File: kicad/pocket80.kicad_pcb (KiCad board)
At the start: 4 copper layers, 68.6 x 107.3 mm, 144 parts, among them J1 USB_C_Receptacle_USB2.0_14P, J2 Conn_02x10_Odd_Even, J3 Conn_01x02, Q1 IRLML6402, Q2 BC847, SW1 F1, SW10 4, SW11 9, SW12 5, SW13 A, SW14 6, SW15 B, SW16 7, SW17 0, SW18 INC, SW19 1, SW2 F2, SW20 DEC, SW21 2, SW22 SEL, SW23 3, SW24 GO!, SW25 SW_Push_DPDT, SW26 RESET, SW3 F3, SW4 F4, SW5 C, SW6 D, SW7 E, SW8 F, SW9 8, U1 Z80CPU, U10 74HC00, U11 74HC138, U12 CH340N, U13 TP4056-42-ESOP8, U14 SX1308, U15 LM393, U16 74HC74, U17 28C256, U18 74HC32, U2 74HC244, U3 Z80 PIO, U4 Z80 SIO3, U5 Z80 CTC, U6 NE555D, U7 74HC04, U8 62256, U9 24C512, Y1 3.6864M

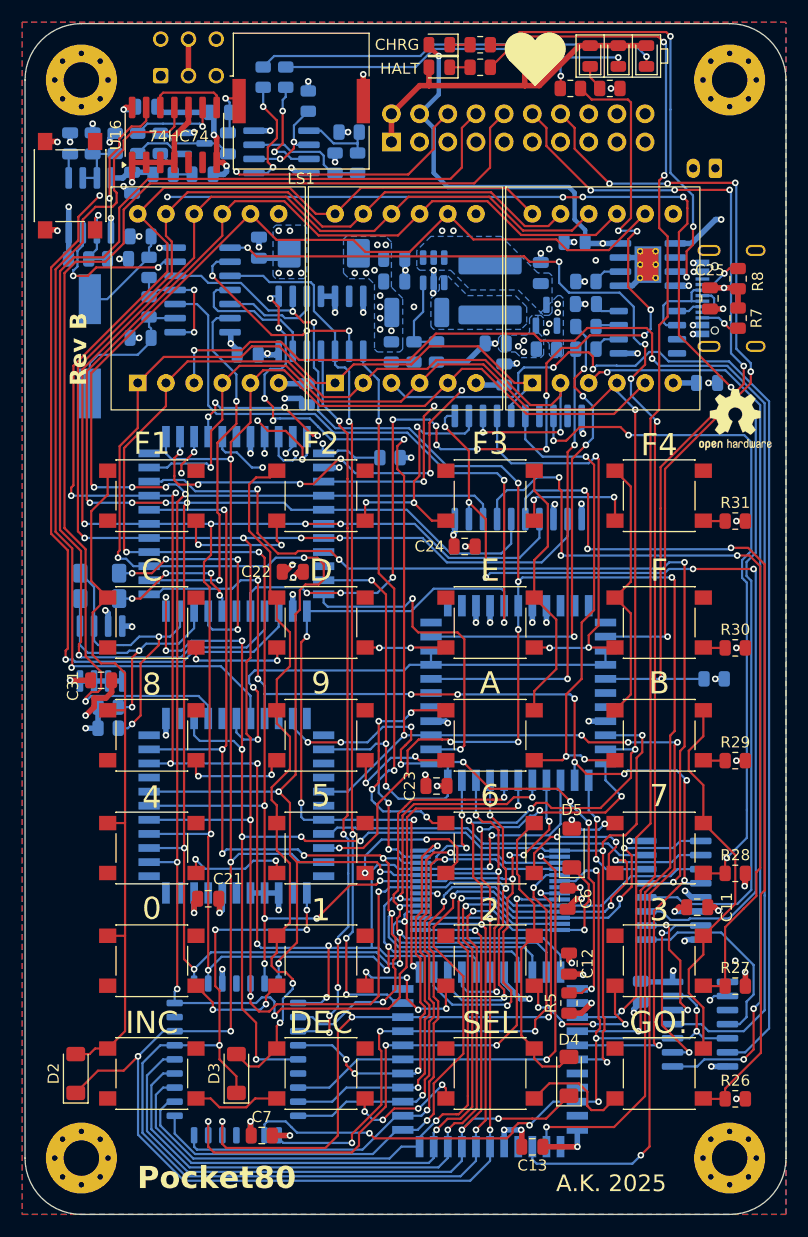
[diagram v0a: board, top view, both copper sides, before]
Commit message: HW: fix floating SYNC pins of SIO
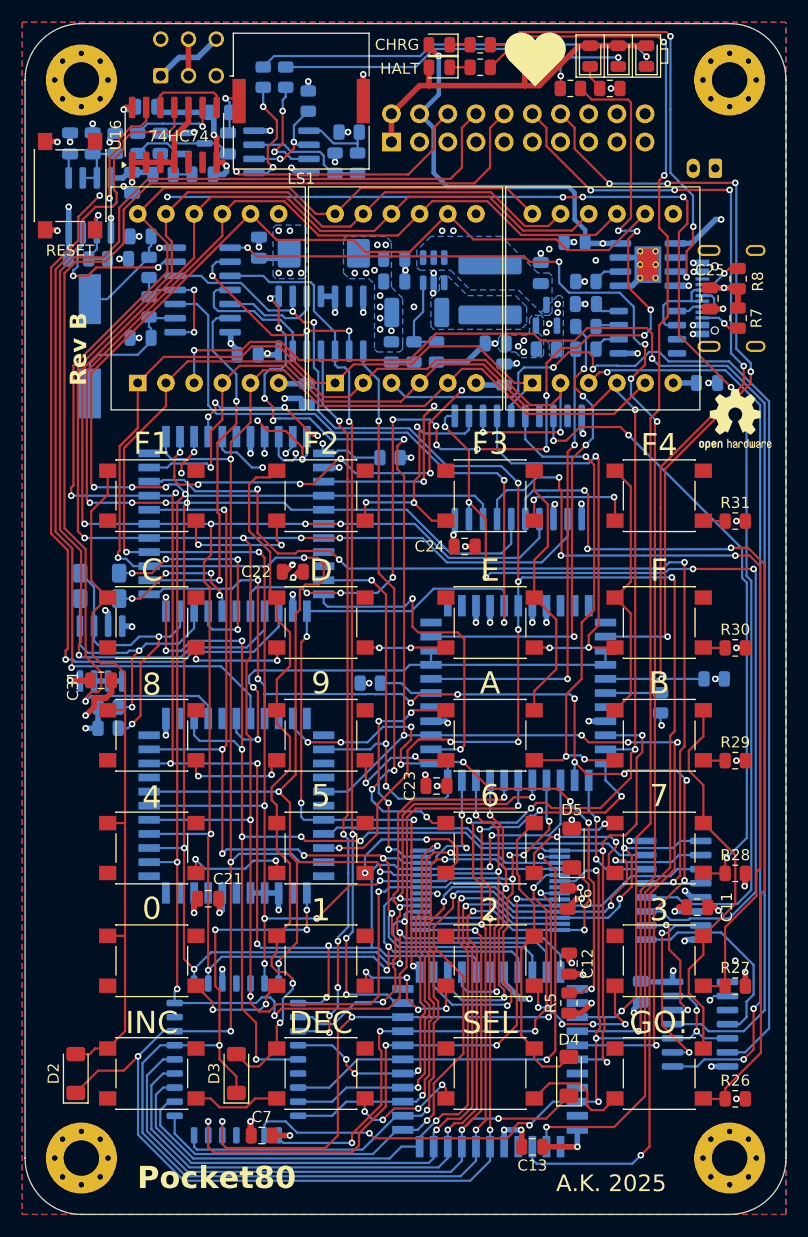
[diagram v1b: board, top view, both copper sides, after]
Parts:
- added R39: 10K, Resistor_SMD:R_0805_2012Metric, B.Cu at (127.6, 94.6)
- added R40: 10K, Resistor_SMD:R_0805_2012Metric, B.Cu at (153.8, 96.4)
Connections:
- U4 pad 12: unconnected-(U4-~{SYNCA}-Pad12) -> Net-(U4-~{SYNCA})
- U4 pad 34: unconnected-(U4-~{SYNCB}-Pad34) -> Net-(U4-~{SYNCB})
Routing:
- net Net-(U2-1A3): track 100.3 -> 93.5 mm
- net +BATT: track 5.89 -> 12.3 mm
- net Net-(U4-~{SYNCB}): track 0.00 -> 4.97 mm
- net Net-(U4-~{SYNCA}): track 0.00 -> 4.93 mm
- net VCC: track 128.7 -> 130.7 mm, vias 46 -> 48
- net /CPU/~{SRST}: track 138.5 -> 137.8 mm
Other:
- board text added: "Pls work"
- board text removed: "JLCJLCJLCJLC"

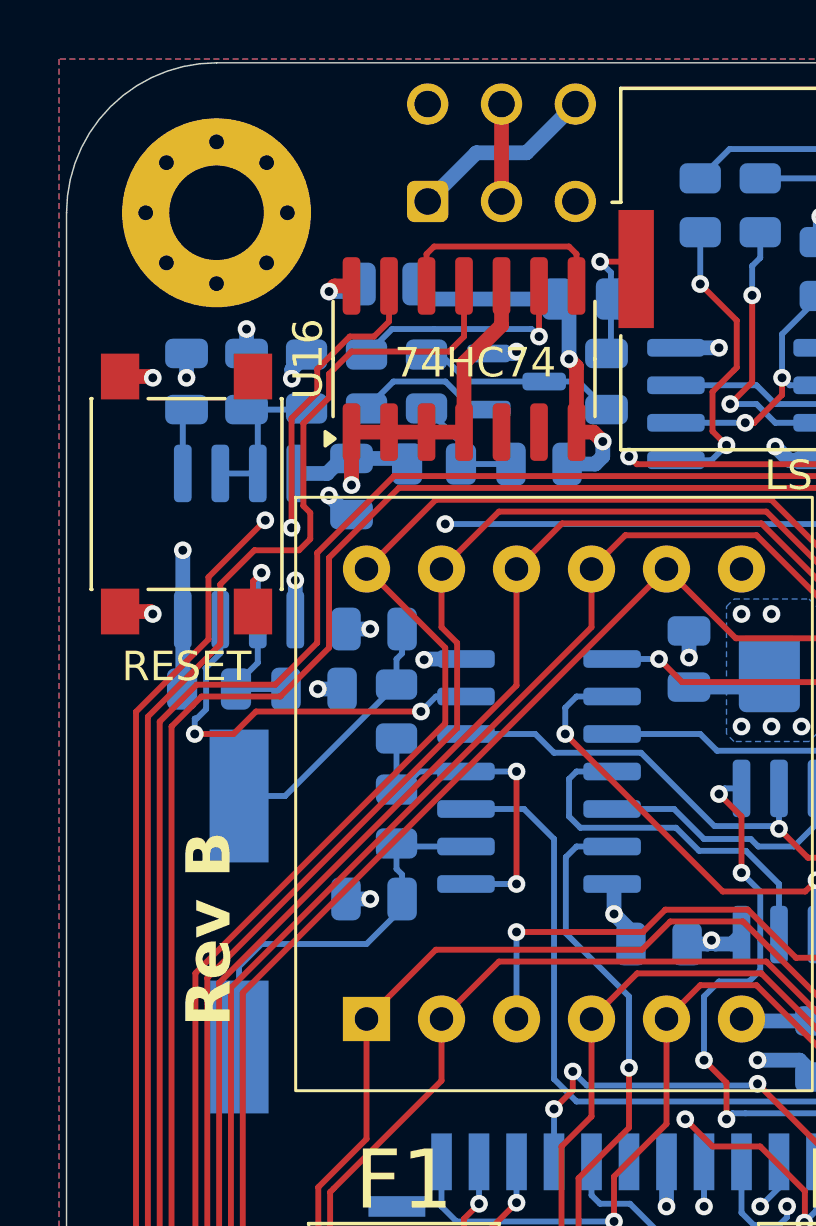
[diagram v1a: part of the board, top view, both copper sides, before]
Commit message: HW: Fix power switch pinout
thx kicad for no coherent pin numeration convention
and random shuffle on footprint assigment...
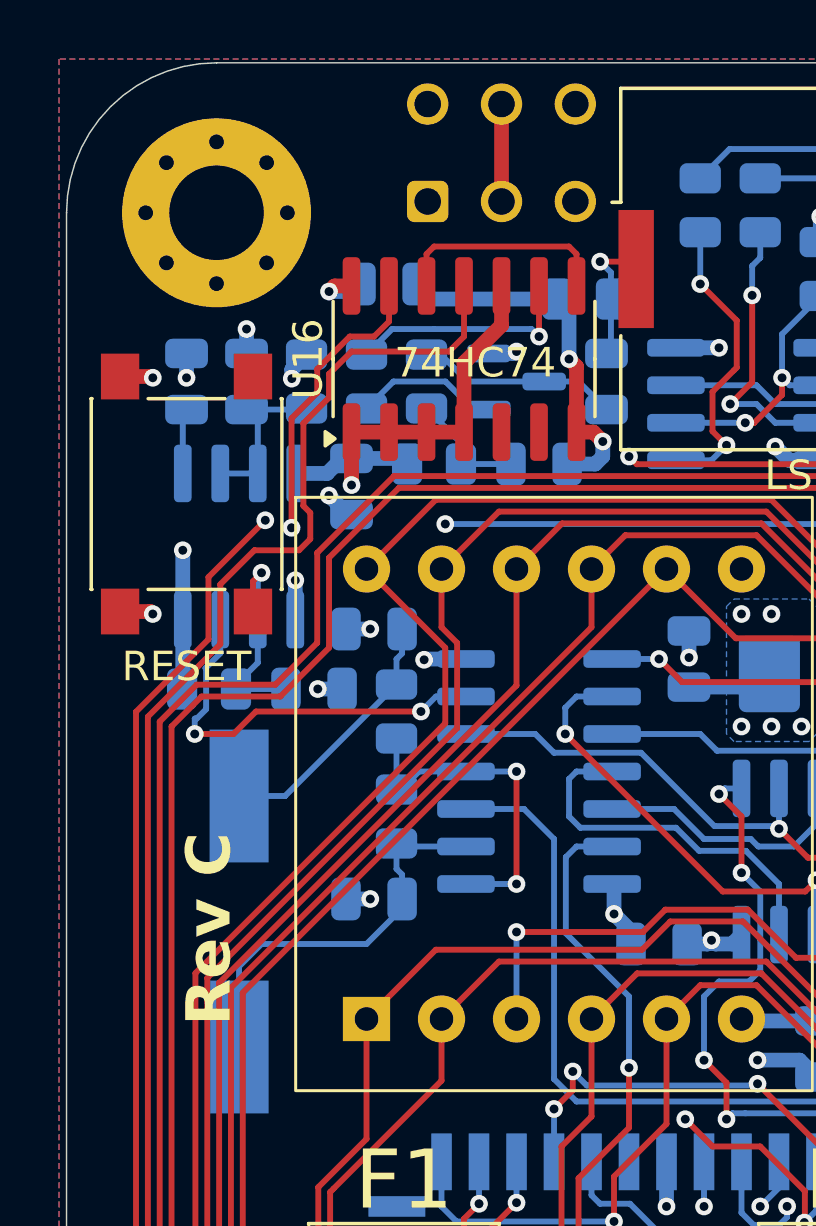
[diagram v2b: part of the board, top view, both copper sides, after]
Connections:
- SW25 pad 4: +BATT -> GND
- SW25 pad 6: GND -> +BATT
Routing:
- net +BATT: track 12.3 -> 5.89 mm
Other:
- board text added: "Rev C"
- board text removed: "Rev B"
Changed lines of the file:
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@@
 	(title_block
 		(title "Pocket80")
-		(date "2025-12-04")
-		(rev "B")
+		(date "2025-12-17")
+		(rev "C")
 		(company "A.K.")
 	)
@@
 			(layers "*.Cu" "*.Mask")
 			(remove_unused_layers no)
-			(net 10 "+BATT")
-			(pinfunction "A")
+			(net 2 "GND")
+			(pinfunction "C")
 			(pintype "passive")
 		)
@@
 			(layers "*.Cu" "*.Mask")
 			(remove_unused_layers no)
-			(net 2 "GND")
-			(pinfunction "C")
+			(net 10 "+BATT")
+			(pinfunction "A")
 			(pintype "passive")
 		)
@@
 		)
 	)
-	(gr_text "Rev B"
+	(gr_text "Rev C"
 		(at 101.346 64.516 90)
 		(layer "F.SilkS")
@@
 	)
 	(segment
-		(start 108.752 39.876)
-		(end 110.401 38.227)
-		(width 0.5)
-		(layer "B.Cu")
-		(net 10)
-	)
-	(segment
-		(start 112.101 38.227)
-		(end 113.752 36.576)
-		(width 0.5)
-		(layer "B.Cu")
-		(net 10)
-	)
-	(segment
 		(start 122.047 41.2515)
 		(end 122.047 40.386)
 		(width 0.5)
 		(layer "B.Cu")
-		(net 10)
-	)
-	(segment
-		(start 110.401 38.227)
-		(end 112.101 38.227)
-		(width 0.5)
-		(layer "B.Cu")

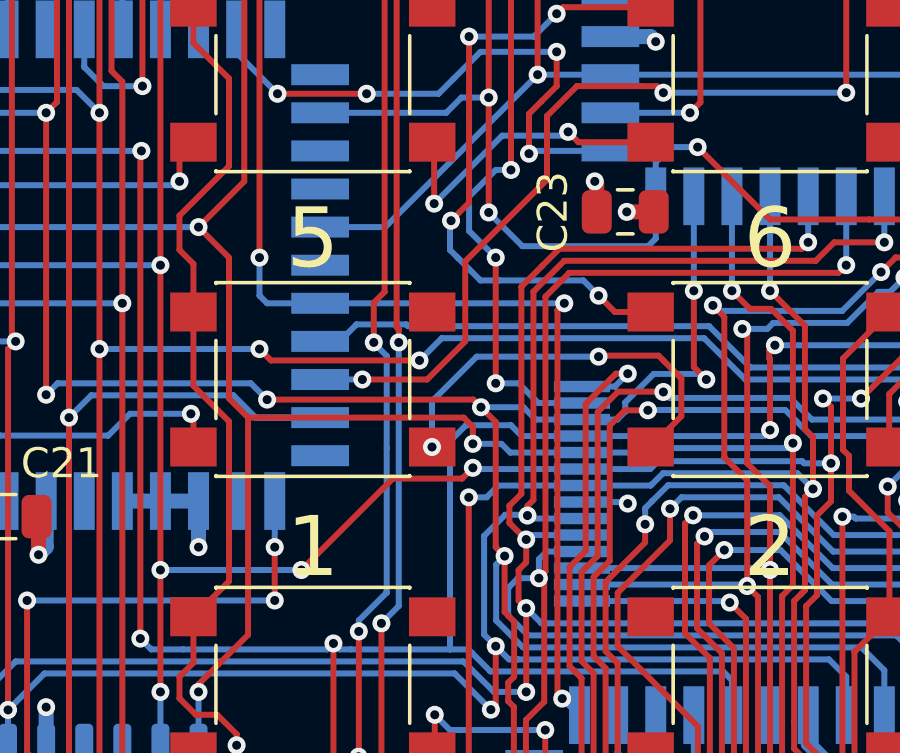
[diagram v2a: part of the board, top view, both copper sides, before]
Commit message: HW: Fix initial IEI not being connected
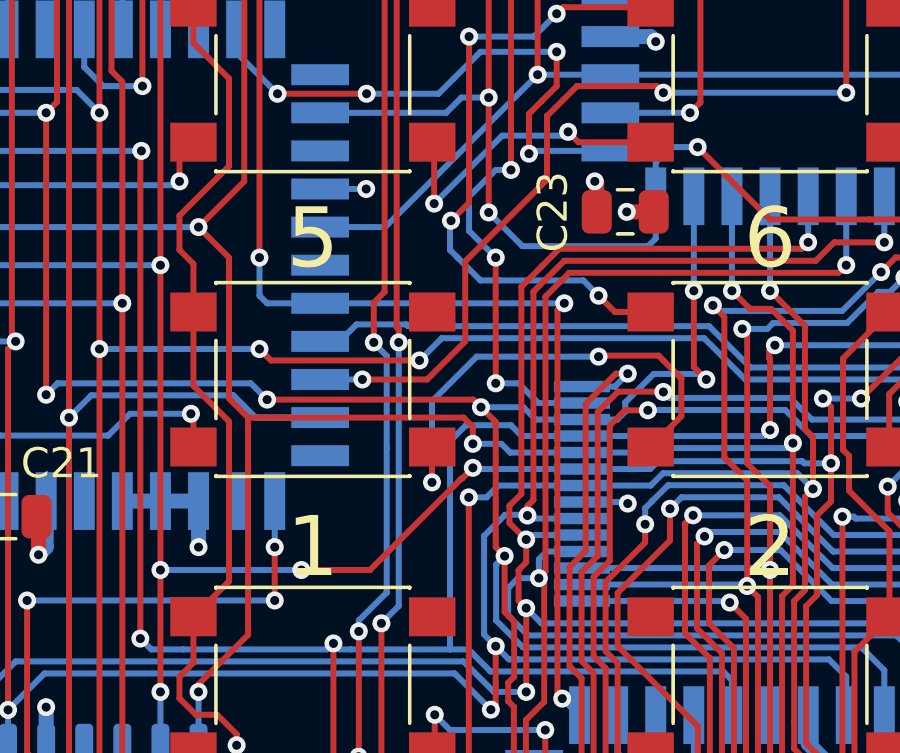
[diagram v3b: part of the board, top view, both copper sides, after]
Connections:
- U5 pad 21: /CTC/IEI -> VCC
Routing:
- net Net-(U2-1A3): track 93.5 -> 95.9 mm
- net VCC: track 130.7 -> 132.2 mm, vias 48 -> 49
